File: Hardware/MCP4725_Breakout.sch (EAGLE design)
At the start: 16 parts, among them U1 DAC_MCP4725SOT-CP

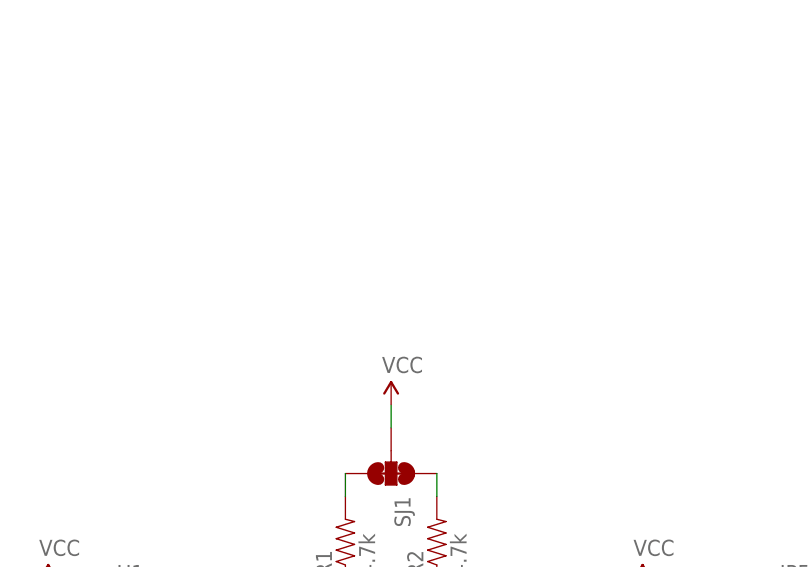
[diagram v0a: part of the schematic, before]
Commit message: Last Commit before Reds
Added my name to brd. file
added Vcc levels to sch.
changed file name so version # isn't there
minor silk fixes due to vias.
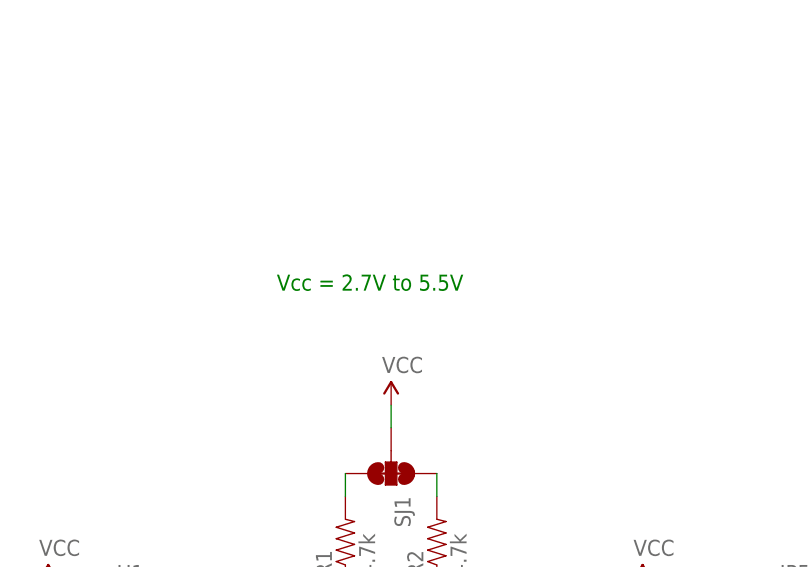
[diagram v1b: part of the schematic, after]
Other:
- note added: "Vcc = 2.7V to 5.5V"
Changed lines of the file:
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@@
 <text x="170.942" y="11.43" size="2.1844" layer="94">Joel Bartlett</text>
 <text x="238.76" y="7.62" size="2.1844" layer="94" ratio="9">14</text>
+<text x="111.76" y="132.08" size="1.778" layer="91">Vcc = 2.7V to 5.5V</text>
 </plain>
 <instances>

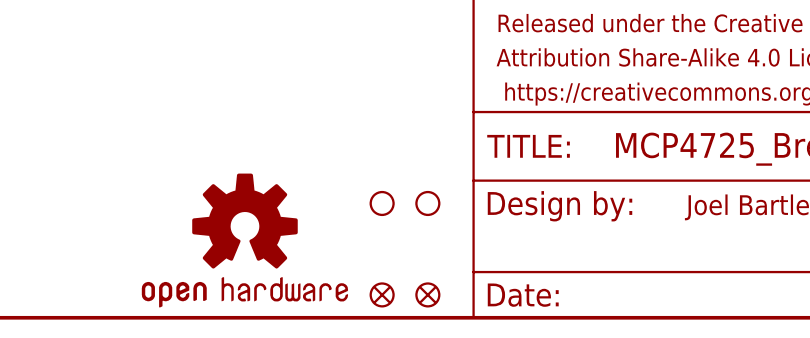
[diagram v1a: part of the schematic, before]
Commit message: removed micro fiducial, added regulars
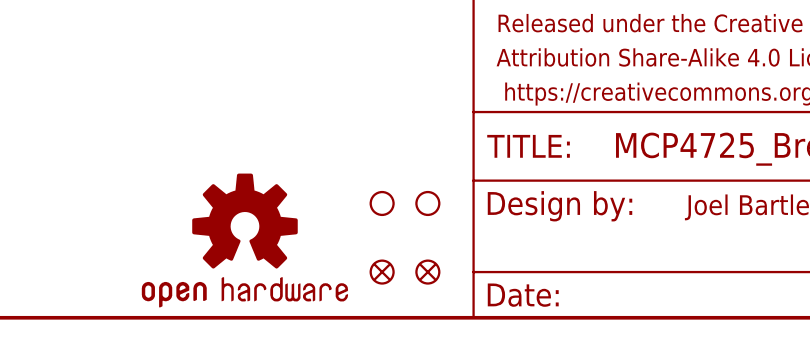
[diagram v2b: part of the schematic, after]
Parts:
- removed JP2, JP3: FIDUCIALUFIDUCIAL, SparkFun:FIDUCIALUFIDUCIAL
- added FID1, FID2: FIDUCIAL1X2, SparkFun-Aesthetics:FIDUCIAL1X2
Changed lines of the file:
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@@
 <?xml version="1.0" encoding="utf-8"?>
 <!DOCTYPE eagle SYSTEM "eagle.dtd">
-<eagle version="6.5.0">
+<eagle version="6.6.0">
 <drawing>
 <settings>
@@
 <part name="P+4" library="SparkFun" deviceset="VCC" device=""/>
 <part name="P+5" library="SparkFun" deviceset="VCC" device=""/>
-<part name="JP2" library="SparkFun" deviceset="FIDUCIAL" device="UFIDUCIAL"/>
-<part name="JP3" library="SparkFun" deviceset="FIDUCIAL" device="UFIDUCIAL"/>
 <part name="U1" library="SparkFun-AnalogIC" deviceset="DAC_MCP4725" device="SOT-CP"/>
 <part name="GND2" library="SparkFun" deviceset="GND" device=""/>
@@
 <part name="SJ2" library="SparkFun-Passives" deviceset="JUMPER-PAD-3-2OF3_NC_BY_PASTE" device="" value=""/>
 <part name="R3" library="SparkFun" deviceset="RESISTOR" device="0603-RES" value="10k"/>
+<part name="FID1" library="SparkFun-Aesthetics" deviceset="FIDUCIAL" device="1X2"/>
+<part name="FID2" library="SparkFun-Aesthetics" deviceset="FIDUCIAL" device="1X2"/>
 </parts>
 <sheets>
@@
 <instance part="P+4" gate="1" x="152.4" y="99.06"/>
 <instance part="P+5" gate="1" x="86.36" y="99.06"/>
-<instance part="JP2" gate="G$1" x="137.16" y="2.54"/>
-<instance part="JP3" gate="G$1" x="142.24" y="2.54"/>
 <instance part="U1" gate="G$1" x="101.6" y="93.98"/>
 <instance part="GND2" gate="1" x="96.52" y="68.58"/>
@@
 <instance part="SJ2" gate="G$1" x="116.84" y="73.66" rot="R270"/>
 <instance part="R3" gate="G$1" x="104.14" y="73.66"/>
+<instance part="FID1" gate="G$1" x="137.16" y="5.08"/>
+<instance part="FID2" gate="G$1" x="142.24" y="5.08"/>
 </instances>
 <busses>

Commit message: Corrected to generic SOT-23 library
See engineering file audit, package issues for more information.
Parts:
- FRAME2: value FRAME-LETTER -> (none)
- U1: value DAC_MCP4725SOT-CP -> MCP4725; device SparkFun-AnalogIC:DAC_MCP4725SOT-CP -> SparkFun-AnalogIC:MCP4725SOT-23
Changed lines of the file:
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@@
 <?xml version="1.0" encoding="utf-8"?>
 <!DOCTYPE eagle SYSTEM "eagle.dtd">
-<eagle version="6.6.0">
+<eagle version="7.2.0">
 <drawing>
 <settings>
@@
 <layer number="56" name="wert" color="7" fill="1" visible="no" active="no"/>
 <layer number="57" name="tCAD" color="7" fill="1" visible="no" active="no"/>
+<layer number="90" name="Modules" color="5" fill="1" visible="no" active="yes"/>
 <layer number="91" name="Nets" color="2" fill="1" visible="yes" active="yes"/>
 <layer number="92" name="Busses" color="1" fill="1" visible="yes" active="yes"/>
@@
 <layer number="251" name="SMDround" color="12" fill="11" visible="no" active="no"/>
 <layer number="254" name="cooling" color="7" fill="1" visible="yes" active="yes"/>
+<layer number="255" name="routoute" color="7" fill="1" visible="yes" active="yes"/>
 </layers>
-<schematic>
+<schematic xreflabel="%F%N/%S" xrefpart="/%S.%C%R">
 <attributes>
 </attributes>
@@
 <part name="P+4" library="SparkFun" deviceset="VCC" device=""/>
 <part name="P+5" library="SparkFun" deviceset="VCC" device=""/>
-<part name="U1" library="SparkFun-AnalogIC" deviceset="DAC_MCP4725" device="SOT-CP"/>
+<part name="U1" library="SparkFun-AnalogIC" deviceset="MCP4725" device="SOT-23" value="MCP4725"/>
 <part name="GND2" library="SparkFun" deviceset="GND" device=""/>
 <part name="P+1" library="SparkFun" deviceset="VCC" device=""/>
@@
 <part name="JP6" library="SparkFun-Connectors" deviceset="M02" device="PTH"/>
 <part name="SJ1" library="SparkFun-Passives" deviceset="JUMPER-PAD-3-NC_BY_TRACE" device=""/>
-<part name="SJ2" library="SparkFun-Passives" deviceset="JUMPER-PAD-3-2OF3_NC_BY_PASTE" device="" value=""/>
+<part name="SJ2" library="SparkFun-Passives" deviceset="JUMPER-PAD-3-2OF3_NC_BY_PASTE" device="" value="JUMPER-PAD-3-2OF3_NC_BY_PASTE"/>
 <part name="R3" library="SparkFun" deviceset="RESISTOR" device="0603-RES" value="10k"/>
 <part name="FID1" library="SparkFun-Aesthetics" deviceset="FIDUCIAL" device="1X2"/>
@@
 <instance part="P+4" gate="1" x="152.4" y="99.06"/>
 <instance part="P+5" gate="1" x="86.36" y="99.06"/>
-<instance part="U1" gate="G$1" x="101.6" y="93.98"/>
+<instance part="U1" gate="U1" x="101.6" y="93.98"/>
 <instance part="GND2" gate="1" x="96.52" y="68.58"/>
 <instance part="P+1" gate="1" x="124.46" y="78.74"/>
@@
 <instance part="STANDOFF2" gate="G$1" x="142.24" y="12.7"/>
 <instance part="FRAME2" gate="G$1" x="0" y="0"/>
-<instance part="FRAME2" gate="G$2" x="147.32" y="0"/>
+<instance part="FRAME2" gate="V" x="147.32" y="0"/>
 <instance part="LOGO1" gate="G$1" x="121.92" y="10.16"/>
 <instance part="JP5" gate="G$1" x="172.72" y="91.44"/>
@@
 <segment>
 <wire x1="83.82" y1="88.9" x2="83.82" y2="93.98" width="0.1524" layer="91"/>
-<wire x1="83.82" y1="93.98" x2="88.9" y2="93.98" width="0.1524" layer="91"/>
+<wire x1="83.82" y1="93.98" x2="91.44" y2="93.98" width="0.1524" layer="91"/>
 <pinref part="GND5" gate="1" pin="GND"/>
-<pinref part="U1" gate="G$1" pin="VSS"/>
+<pinref part="U1" gate="U1" pin="VSS"/>
 <pinref part="JP6" gate="G$1" pin="1"/>
 <wire x1="71.12" y1="93.98" x2="83.82" y2="93.98" width="0.1524" layer="91"/>
@@
 <net name="VCC" class="0">
 <segment>
-<wire x1="88.9" y1="91.44" x2="86.36" y2="91.44" width="0.1524" layer="91"/>
+<wire x1="91.44" y1="91.44" x2="86.36" y2="91.44" width="0.1524" layer="91"/>
 <wire x1="86.36" y1="91.44" x2="86.36" y2="99.06" width="0.1524" layer="91"/>
 <pinref part="P+5" gate="1" pin="VCC"/>
-<pinref part="U1" gate="G$1" pin="VDD"/>
+<pinref part="U1" gate="U1" pin="VDD"/>
 </segment>
 <segment>
@@
 <net name="SCL" class="0">
 <segment>
-<wire x1="114.3" y1="93.98" x2="119.38" y2="93.98" width="0.1524" layer="91"/>
+<wire x1="111.76" y1="93.98" x2="119.38" y2="93.98" width="0.1524" layer="91"/>
 <wire x1="119.38" y1="93.98" x2="119.38" y2="99.06" width="0.1524" layer="91"/>
 <wire x1="119.38" y1="93.98" x2="132.08" y2="93.98" width="0.1524" layer="91"/>
@@
 <pinref part="R1" gate="G$1" pin="1"/>
 <label x="132.08" y="93.98" size="1.27" layer="95" xref="yes"/>
-<pinref part="U1" gate="G$1" pin="SCL"/>
+<pinref part="U1" gate="U1" pin="SCL"/>
 </segment>
 <segment>
@@
 <net name="SDA" class="0">
 <segment>
-<wire x1="114.3" y1="91.44" x2="129.54" y2="91.44" width="0.1524" layer="91"/>
+<wire x1="111.76" y1="91.44" x2="129.54" y2="91.44" width="0.1524" layer="91"/>
 <wire x1="129.54" y1="91.44" x2="129.54" y2="99.06" width="0.1524" layer="91"/>
 <wire x1="129.54" y1="91.44" x2="132.08" y2="91.44" width="0.1524" layer="91"/>
@@
 <pinref part="R2" gate="G$1" pin="1"/>
 <label x="132.08" y="91.44" size="1.27" layer="95" xref="yes"/>
-<pinref part="U1" gate="G$1" pin="SDA"/>
+<pinref part="U1" gate="U1" pin="SDA"/>
 </segment>
 <segment>
@@
 <net name="N$3" class="0">
 <segment>
-<wire x1="114.3" y1="96.52" x2="116.84" y2="96.52" width="0.1524" layer="91"/>
+<wire x1="111.76" y1="96.52" x2="116.84" y2="96.52" width="0.1524" layer="91"/>
 <wire x1="116.84" y1="96.52" x2="116.84" y2="78.74" width="0.1524" layer="91"/>
-<pinref part="U1" gate="G$1" pin="AO"/>
+<pinref part="U1" gate="U1" pin="AO"/>
 <pinref part="SJ2" gate="G$1" pin="2"/>
 </segment>
@@
 <net name="VOUT" class="0">
 <segment>
-<pinref part="U1" gate="G$1" pin="VOUT"/>
+<pinref part="U1" gate="U1" pin="VOUT"/>
 <pinref part="JP6" gate="G$1" pin="2"/>
-<wire x1="88.9" y1="96.52" x2="71.12" y2="96.52" width="0.1524" layer="91"/>
-</segment>
-</net>
+<wire x1="91.44" y1="96.52" x2="71.12" y2="96.52" width="0.1524" layer="91"/>
+</segment>
+</net>
